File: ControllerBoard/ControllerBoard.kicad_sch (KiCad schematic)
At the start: 0 parts

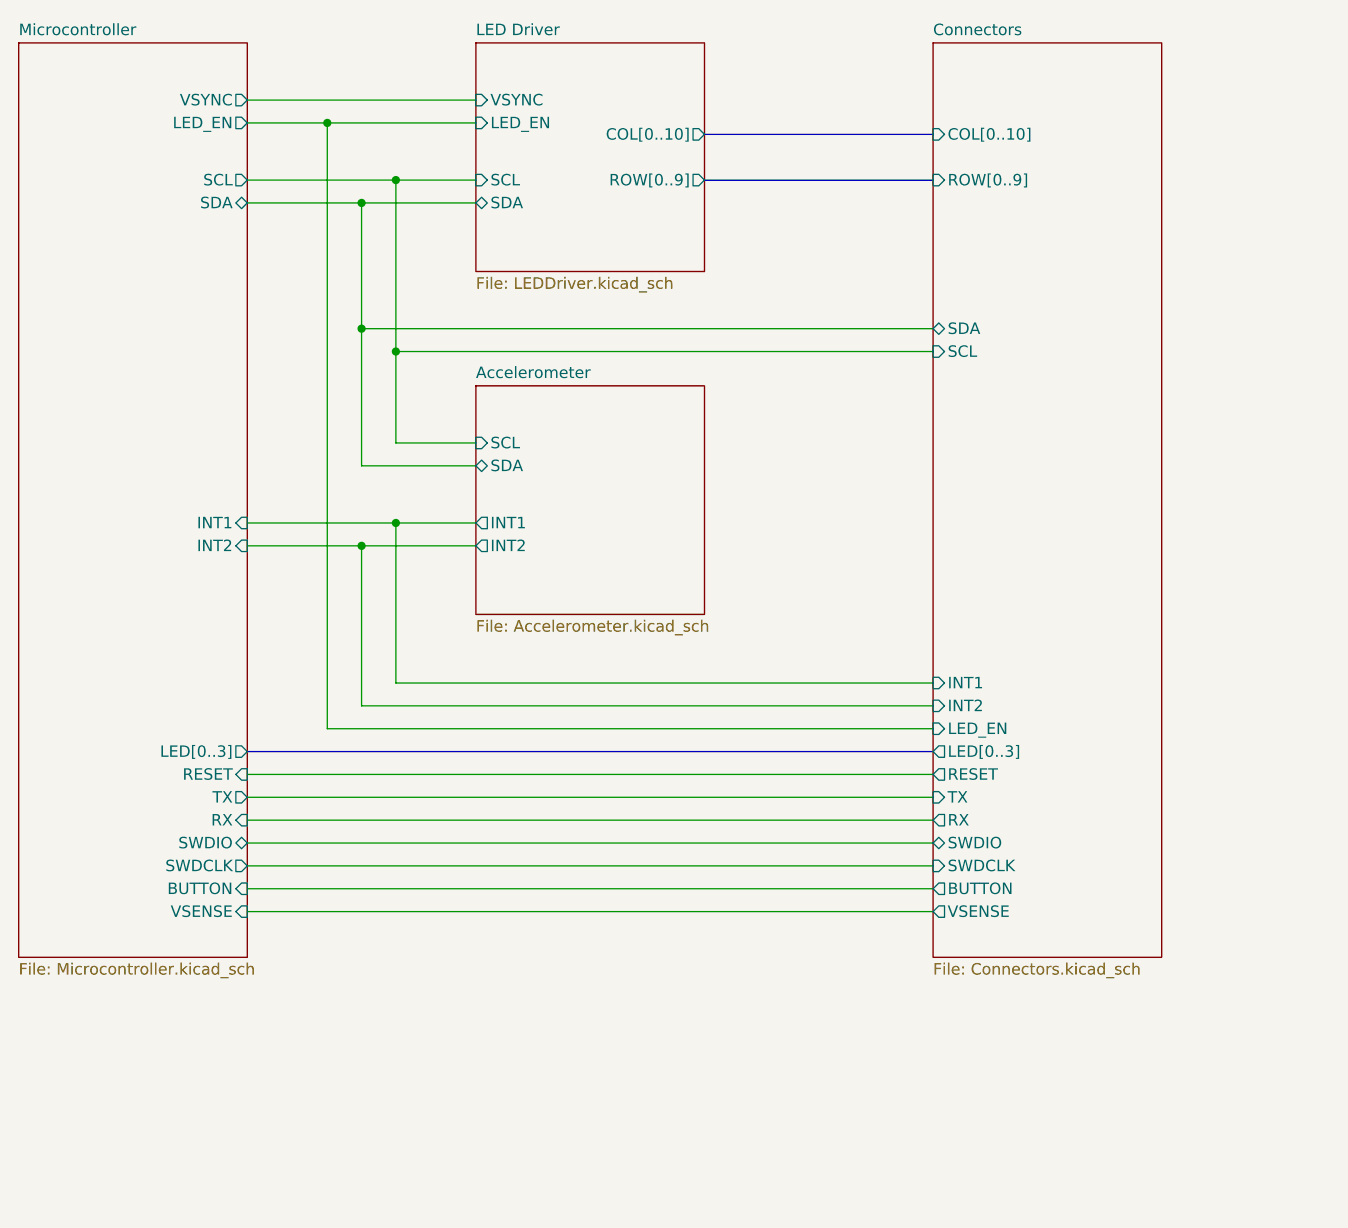
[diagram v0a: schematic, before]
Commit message: Remove LED driver
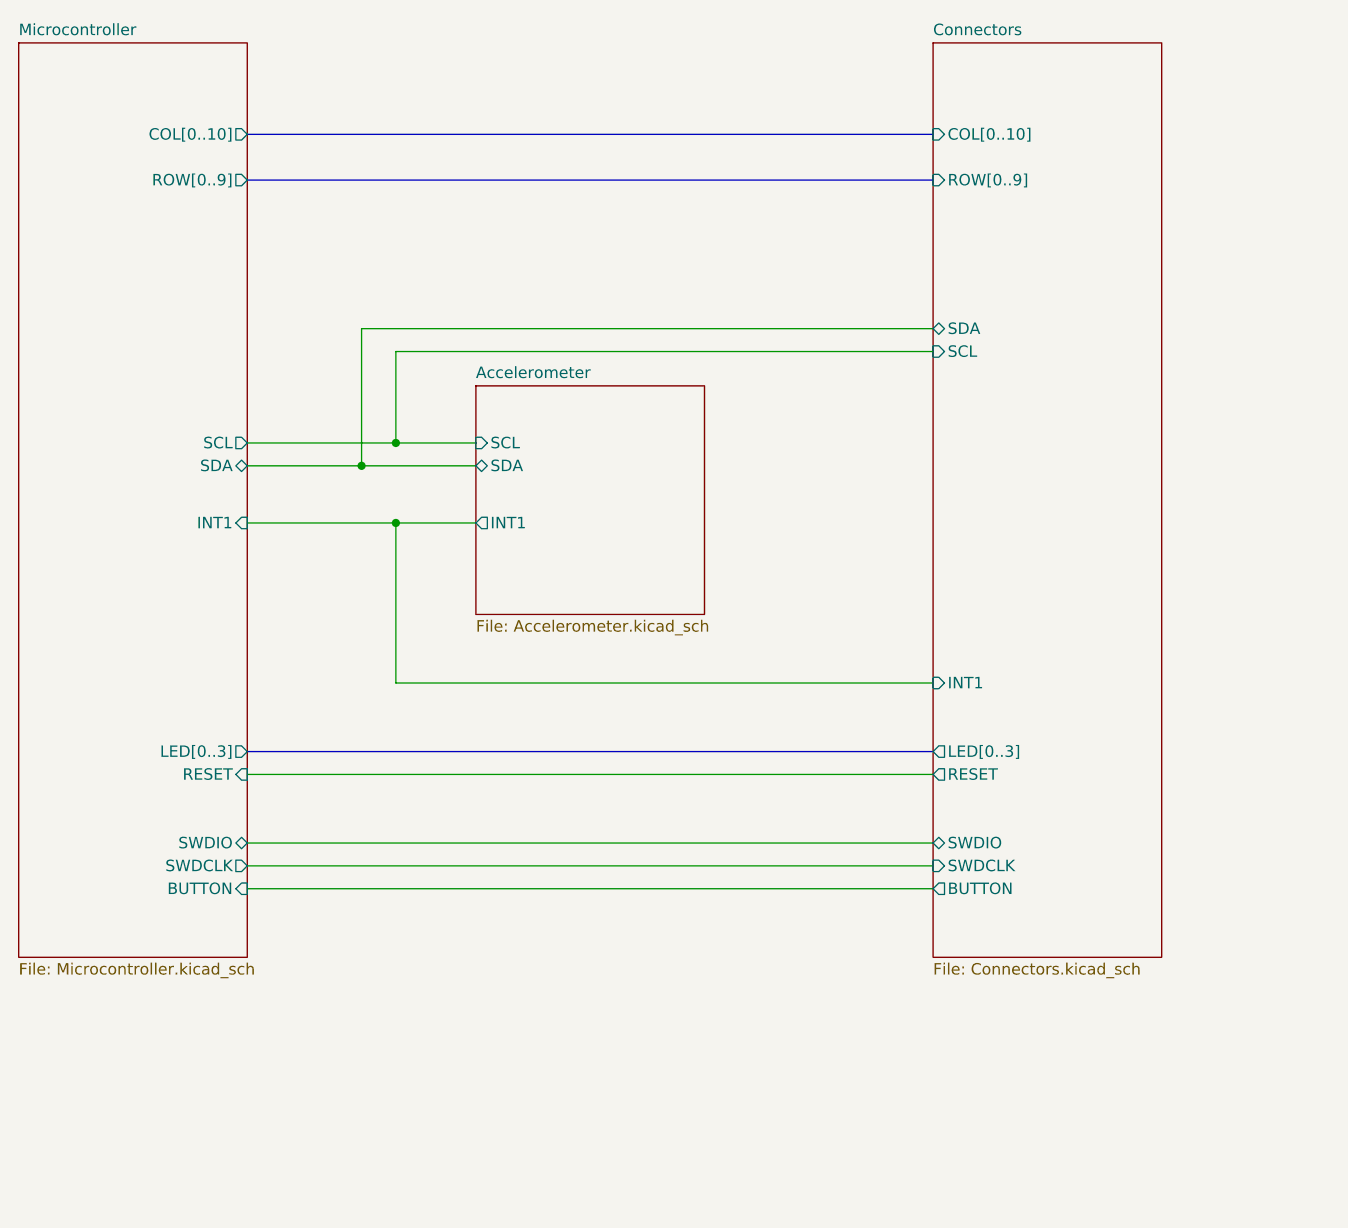
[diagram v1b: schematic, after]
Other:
- removed sheet LED Driver
- sheet Accelerometer ports: added none; removed INT2
- sheet Connectors ports: added none; removed INT2, LED_EN, RX, TX, VSENSE
- sheet Microcontroller ports: added COL[0..10], ROW[0..9]; removed INT2, LED_EN, RX, TX, VSENSE, VSYNC
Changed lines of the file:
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@@
 (kicad_sch (version 20230121) (generator eeschema)
   (paper "A4")
-  (junction (at 59.69 34.29) (diameter 0) (color 0 0 0 0)
+  (junction (at 67.31 69.85) (diameter 0) (color 0 0 0 0)
   )
-  (junction (at 67.31 59.69) (diameter 0) (color 0 0 0 0)
-  )
-  (junction (at 63.5 81.28) (diameter 0) (color 0 0 0 0)
-  )
-  (junction (at 63.5 43.18) (diameter 0) (color 0 0 0 0)
+  (junction (at 63.5 72.39) (diameter 0) (color 0 0 0 0)
   )
   (junction (at 67.31 78.74) (diameter 0) (color 0 0 0 0)
   )
-  (junction (at 67.31 40.64) (diameter 0) (color 0 0 0 0)
+  (wire (pts (xy 50.8 78.74) (xy 67.31 78.74))
+    (stroke (width 0) (type default))
   )
-  (junction (at 63.5 57.15) (diameter 0) (color 0 0 0 0)
-  )
-  (wire (pts (xy 50.8 78.74) (xy 67.31 78.74))
+  (bus (pts (xy 50.8 35.56) (xy 127 35.56))
     (stroke (width 0) (type default))
   )
@@
     (stroke (width 0) (type default))
   )
-  (wire (pts (xy 67.31 40.64) (xy 76.2 40.64))
-    (stroke (width 0) (type default))
-  )
-  (wire (pts (xy 63.5 57.15) (xy 63.5 43.18))
-    (stroke (width 0) (type default))
-  )
-  (wire (pts (xy 67.31 59.69) (xy 67.31 40.64))
-    (stroke (width 0) (type default))
-  )
-  (wire (pts (xy 50.8 109.22) (xy 127 109.22))
-    (stroke (width 0) (type default))
-  )
   (wire (pts (xy 50.8 119.38) (xy 127 119.38))
     (stroke (width 0) (type default))
   )
-  (wire (pts (xy 63.5 43.18) (xy 76.2 43.18))
-    (stroke (width 0) (type default))
-  )
   (wire (pts (xy 67.31 69.85) (xy 67.31 59.69))
-    (stroke (width 0) (type default))
-  )
-  (wire (pts (xy 50.8 31.75) (xy 76.2 31.75))
-    (stroke (width 0) (type default))
-  )
-  (wire (pts (xy 59.69 34.29) (xy 76.2 34.29))
     (stroke (width 0) (type default))
   )
@@
     (stroke (width 0) (type default))
   )
-  (wire (pts (xy 63.5 99.06) (xy 63.5 81.28))
-    (stroke (width 0) (type default))
-  )
   (bus (pts (xy 50.8 104.14) (xy 127 104.14))
     (stroke (width 0) (type default))
@@
     (stroke (width 0) (type default))
   )
-  (wire (pts (xy 127 101.6) (xy 59.69 101.6))
+  (wire (pts (xy 50.8 72.39) (xy 63.5 72.39))
     (stroke (width 0) (type default))
   )
-  (wire (pts (xy 59.69 101.6) (xy 59.69 34.29))
-    (stroke (width 0) (type default))
-  )
-  (wire (pts (xy 50.8 43.18) (xy 63.5 43.18))
-    (stroke (width 0) (type default))
-  )
-  (wire (pts (xy 50.8 111.76) (xy 127 111.76))
-    (stroke (width 0) (type default))
-  )
-  (bus (pts (xy 101.6 40.64) (xy 127 40.64))
-    (stroke (width 0) (type default))
-  )
-  (wire (pts (xy 50.8 81.28) (xy 63.5 81.28))
+  (bus (pts (xy 50.8 40.64) (xy 127 40.64))
     (stroke (width 0) (type default))
   )
@@
     (stroke (width 0) (type default))
   )
-  (wire (pts (xy 50.8 121.92) (xy 127 121.92))
-    (stroke (width 0) (type default))
-  )
-  (wire (pts (xy 50.8 40.64) (xy 67.31 40.64))
-    (stroke (width 0) (type default))
-  )
-  (wire (pts (xy 50.8 34.29) (xy 59.69 34.29))
+  (wire (pts (xy 50.8 69.85) (xy 67.31 69.85))
     (stroke (width 0) (type default))
   )
@@
     (stroke (width 0) (type default))
   )
-  (bus (pts (xy 101.6 35.56) (xy 127 35.56))
-    (stroke (width 0) (type default))
-  )
-  (wire (pts (xy 127 99.06) (xy 63.5 99.06))
-    (stroke (width 0) (type default))
-  )
   (wire (pts (xy 50.8 114.3) (xy 127 114.3))
-    (stroke (width 0) (type default))
-  )
-  (wire (pts (xy 63.5 81.28) (xy 76.2 81.28))
     (stroke (width 0) (type default))
   )
@@
       (effects (font (size 1.27 1.27)) (justify left))
     )
-    (pin "RX" output (at 127 111.76 180)
-      (effects (font (size 1.27 1.27)) (justify left))
-    )
     (pin "RESET" output (at 127 106.68 180)
-      (effects (font (size 1.27 1.27)) (justify left))
-    )
-    (pin "TX" input (at 127 109.22 180)
-      (effects (font (size 1.27 1.27)) (justify left))
-    )
-    (pin "VSENSE" output (at 127 121.92 180)
       (effects (font (size 1.27 1.27)) (justify left))
     )
@@
       (effects (font (size 1.27 1.27)) (justify left))
     )
-    (pin "LED_EN" input (at 127 101.6 180)
-      (effects (font (size 1.27 1.27)) (justify left))
-    )
-    (pin "INT2" input (at 127 99.06 180)
-      (effects (font (size 1.27 1.27)) (justify left))
-    )
     (pin "INT1" input (at 127 96.52 180)
       (effects (font (size 1.27 1.27)) (justify left))
@@
     (instances
       (project "ControllerBoard"
-        (path "/61399469-98b3-4896-9e05-807fdca9097a" (page "5"))
+        (path "/61399469-98b3-4896-9e05-807fdca9097a" (page "4"))
       )
     )
@@
       (effects (font (size 1.27 1.27)) (justify left top))
     )
-    (pin "SDA" bidirectional (at 50.8 43.18 0)
+    (pin "SDA" bidirectional (at 50.8 72.39 0)
       (effects (font (size 1.27 1.27)) (justify right))
     )
-    (pin "SCL" output (at 50.8 40.64 0)
-      (effects (font (size 1.27 1.27)) (justify right))
-    )
-    (pin "VSYNC" output (at 50.8 31.75 0)
-      (effects (font (size 1.27 1.27)) (justify right))
-    )
-    (pin "LED_EN" output (at 50.8 34.29 0)
+    (pin "SCL" output (at 50.8 69.85 0)
       (effects (font (size 1.27 1.27)) (justify right))
     )
@@
       (effects (font (size 1.27 1.27)) (justify right))
     )
-    (pin "INT2" input (at 50.8 81.28 0)
-      (effects (font (size 1.27 1.27)) (justify right))
-    )
-    (pin "VSENSE" input (at 50.8 121.92 0)
-      (effects (font (size 1.27 1.27)) (justify right))
-    )
     (pin "SWDCLK" output (at 50.8 116.84 0)
       (effects (font (size 1.27 1.27)) (justify right))
@@
       (effects (font (size 1.27 1.27)) (justify right))
     )
-    (pin "TX" output (at 50.8 109.22 0)
+    (pin "ROW[0..9]" output (at 50.8 40.64 0)
       (effects (font (size 1.27 1.27)) (justify right))
     )
-    (pin "RX" input (at 50.8 111.76 0)
+    (pin "COL[0..10]" output (at 50.8 35.56 0)
       (effects (font (size 1.27 1.27)) (justify right))
     )
@@
     )
   )
-  (sheet (at 76.2 25.4) (size 25.4 25.4) (fields_autoplaced)
-    (stroke (width 0.1524) (type solid))
-    (fill (color 0 0 0 0.0000))
-    (property "Sheetname" "LED Driver" (at 76.2 24.6884 0)
-      (effects (font (size 1.27 1.27)) (justify left bottom))
-    )
-    (property "Sheetfile" "LEDDriver.kicad_sch" (at 76.2 51.3846 0)
-      (effects (font (size 1.27 1.27)) (justify left top))
-    )
-    (pin "VSYNC" input (at 76.2 31.75 180)
-      (effects (font (size 1.27 1.27)) (justify left))
-    )
-    (pin "SCL" input (at 76.2 40.64 180)
-      (effects (font (size 1.27 1.27)) (justify left))
-    )
-    (pin "SDA" bidirectional (at 76.2 43.18 180)
-      (effects (font (size 1.27 1.27)) (justify left))
-    )
-    (pin "LED_EN" input (at 76.2 34.29 180)
-      (effects (font (size 1.27 1.27)) (justify left))
-    )
-    (pin "COL[0..10]" output (at 101.6 35.56 0)
-      (effects (font (size 1.27 1.27)) (justify right))
-    )
-    (pin "ROW[0..9]" output (at 101.6 40.64 0)
-      (effects (font (size 1.27 1.27)) (justify right))
-    )
-    (instances
-      (project "WordClock"
-        (path "/69c898ea-1166-4176-b676-6047012e211c" (page "7"))
-        (path "/69c898ea-1166-4176-b676-6047012e211c/70f18072-0a0e-4fb9-8bc7-2b36cbd2fbf6" (page "4"))
-        (path "/69c898ea-1166-4176-b676-6047012e211c/b81512ca-56d9-4472-a200-8f9fd04701de" (page "4"))
-      )
-      (project "ControllerBoard"
-        (path "/61399469-98b3-4896-9e05-807fdca9097a" (page "3"))
-      )
-    )
-  )
   (sheet (at 76.2 63.5) (size 25.4 25.4) (fields_autoplaced)
     (stroke (width 0.1524) (type solid))
@@
     (property "Sheetfile" "Accelerometer.kicad_sch" (at 76.2 89.4846 0)
       (effects (font (size 1.27 1.27)) (justify left top))
-    )
-    (pin "INT2" output (at 76.2 81.28 180)
-      (effects (font (size 1.27 1.27)) (justify left))
     )
     (pin "INT1" output (at 76.2 78.74 180)
@@
       )
       (project "ControllerBoard"
-        (path "/61399469-98b3-4896-9e05-807fdca9097a" (page "4"))
+        (path "/61399469-98b3-4896-9e05-807fdca9097a" (page "3"))
       )
     )
